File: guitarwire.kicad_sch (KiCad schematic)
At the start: 9 parts, among them J1 JACK_OUT

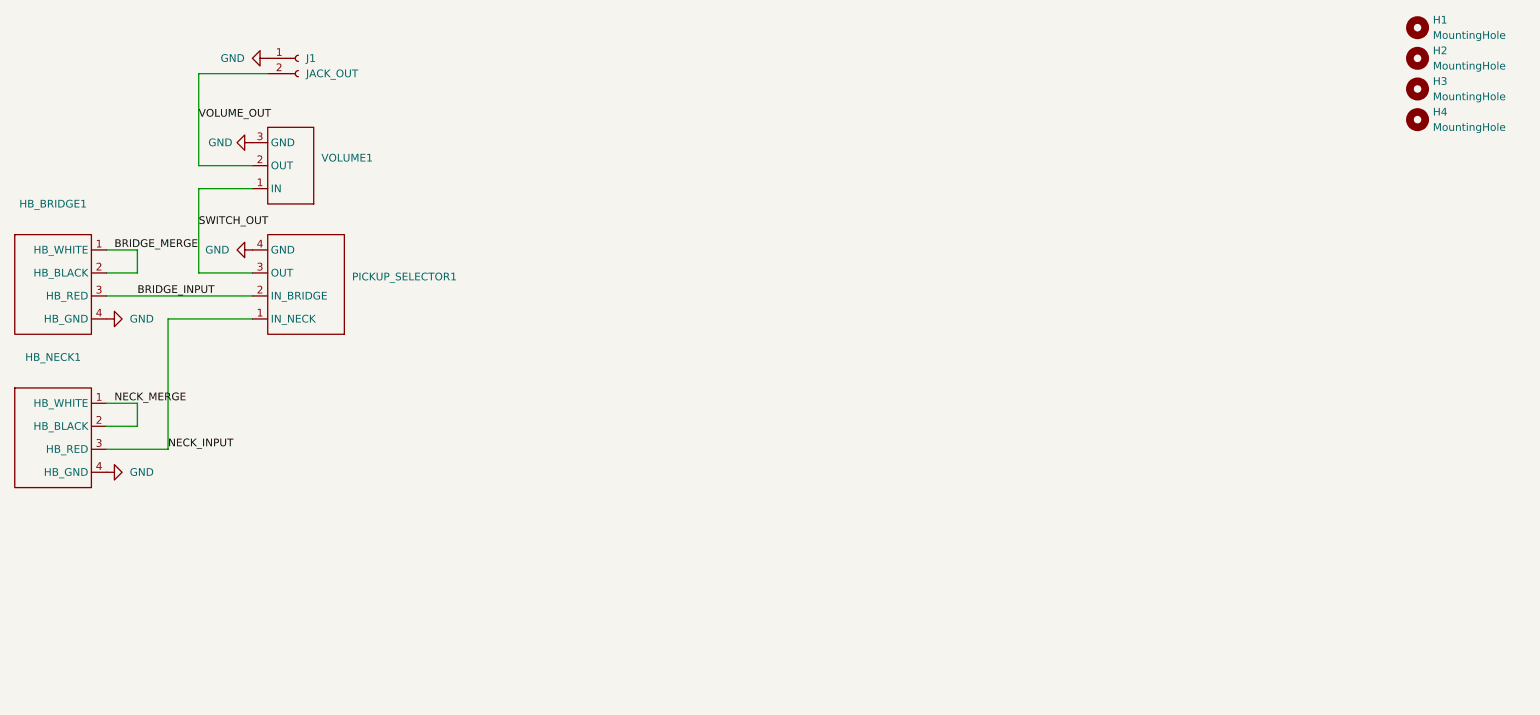
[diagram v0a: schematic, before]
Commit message: Redesign board to use JST XH connectors.
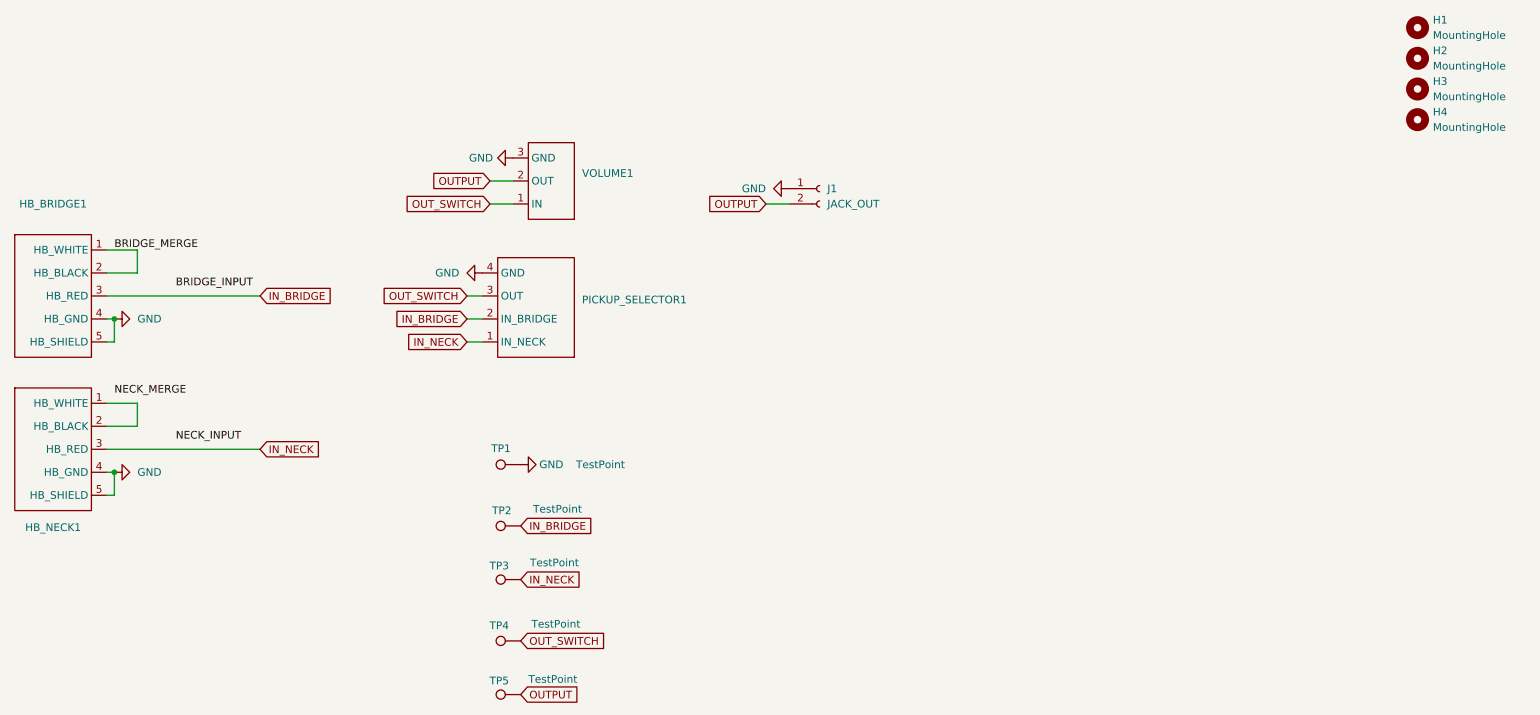
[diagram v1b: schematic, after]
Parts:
- added TP1, TP2, TP3, TP4, TP5: TestPoint, TestPoint:TestPoint_THTPad_2.0x2.0mm_Drill1.0mm, symbol Connector:TestPoint
- HB_BRIDGE1, HB_NECK1: footprint TerminalBlock_Phoenix:TerminalBlock_Phoenix_MKDS-1,5-4-5.08_1x04_P5.08mm_Horizontal -> Connector_JST:JST_XH_B5B-XH-AM_1x05_P2.50mm_Vertical
- J1: footprint TerminalBlock_Phoenix:TerminalBlock_Phoenix_MKDS-1,5-2-5.08_1x02_P5.08mm_Horizontal -> Connector_JST:JST_XH_B2B-XH-AM_1x02_P2.50mm_Vertical
- PICKUP_SELECTOR1: footprint TerminalBlock_Phoenix:TerminalBlock_Phoenix_MKDS-1,5-4-5.08_1x04_P5.08mm_Horizontal -> Connector_JST:JST_XH_B4B-XH-AM_1x04_P2.50mm_Vertical
- VOLUME1: footprint TerminalBlock_Phoenix:TerminalBlock_Phoenix_MKDS-1,5-3-5.08_1x03_P5.08mm_Horizontal -> Connector_JST:JST_XH_B3B-XH-AM_1x03_P2.50mm_Vertical
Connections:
- net BRIDGE_INPUT: no longer HB_BRIDGE1.3 (HB_RED), PICKUP_SELECTOR1.2 (IN_BRIDGE)
- net GND: now also HB_BRIDGE1.5 (HB_SHIELD), HB_NECK1.5 (HB_SHIELD), TP1.1
- net NECK_INPUT: no longer HB_NECK1.3 (HB_RED), PICKUP_SELECTOR1.1 (IN_NECK)
- net NECK_MERGE: no longer HB_NECK1.1 (HB_WHITE), HB_NECK1.2 (HB_BLACK)
- net SWITCH_OUT renamed OUT_SWITCH
- net OUT_SWITCH: now also TP4.1
- net VOLUME_OUT renamed OUTPUT
- net OUTPUT: now also TP5.1
- new net: HB_NECK1.1 (HB_WHITE), HB_NECK1.2 (HB_BLACK)
- new net IN_BRIDGE: HB_BRIDGE1.3 (HB_RED), PICKUP_SELECTOR1.2 (IN_BRIDGE), TP2.1
- new net IN_NECK: HB_NECK1.3 (HB_RED), PICKUP_SELECTOR1.1 (IN_NECK), TP3.1
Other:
- moved on the sheet: J1, PICKUP_SELECTOR1, VOLUME1
